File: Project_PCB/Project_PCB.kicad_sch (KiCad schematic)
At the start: 14 parts, among them J1 USB_C_Receptacle, J2 Conn_01x03_Socket, U1 ESP32-WROOM-32E

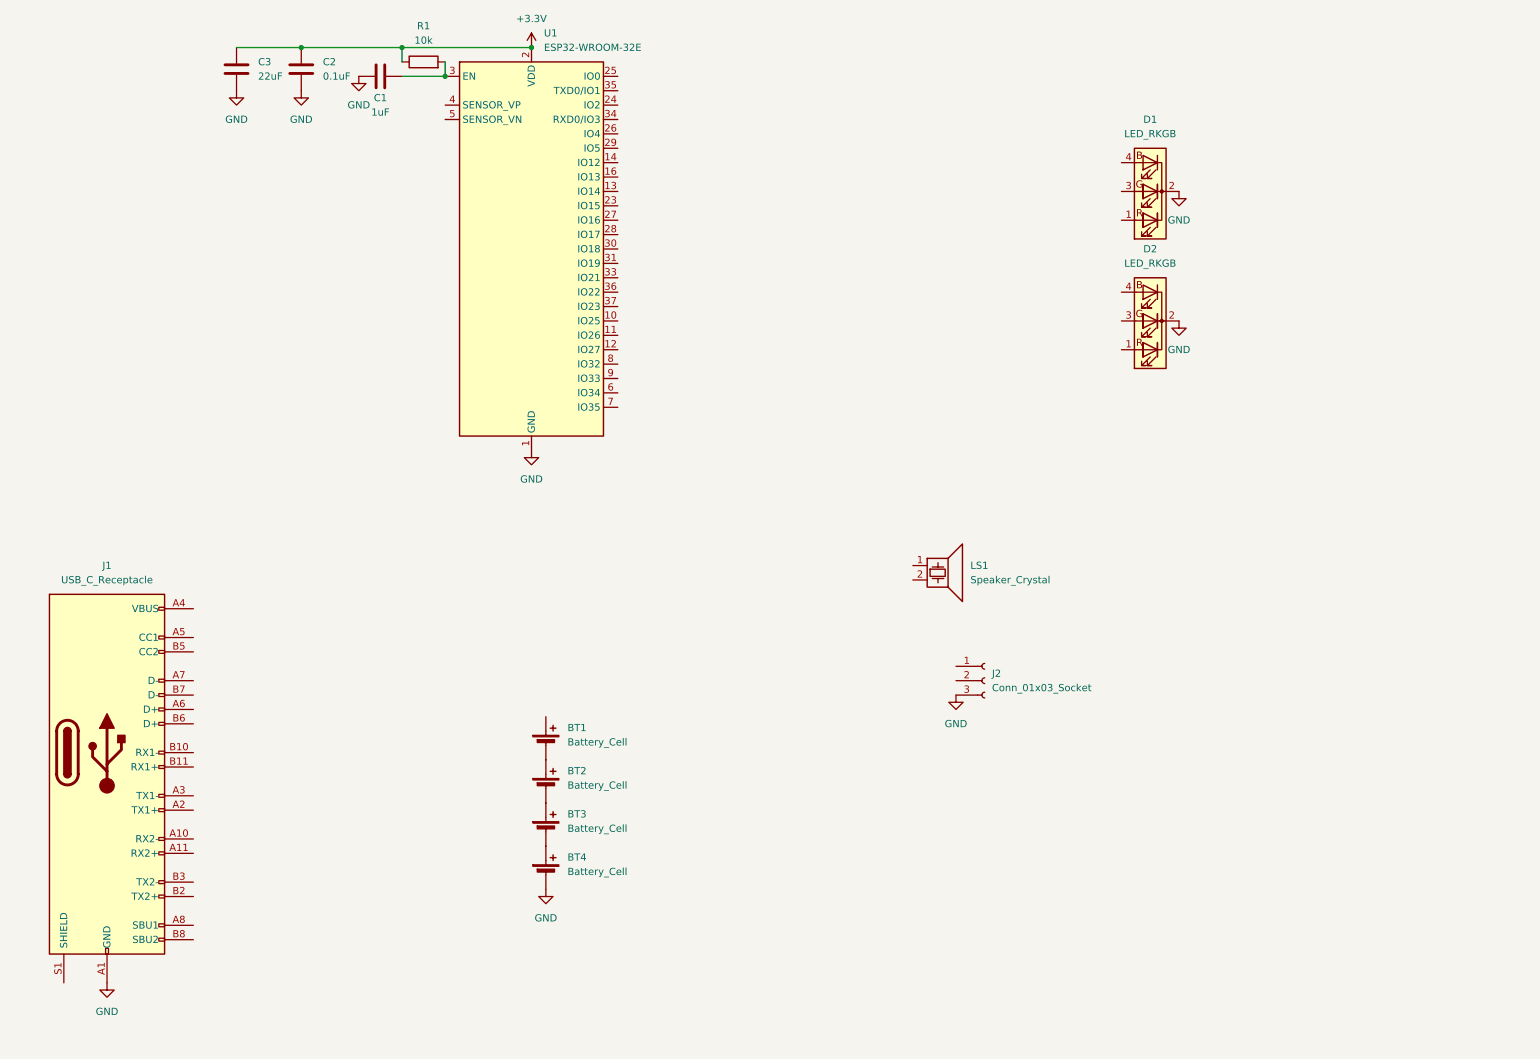
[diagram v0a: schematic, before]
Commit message: Changed mcu to ESP32-S3-WROOM-1 and updated some connections.
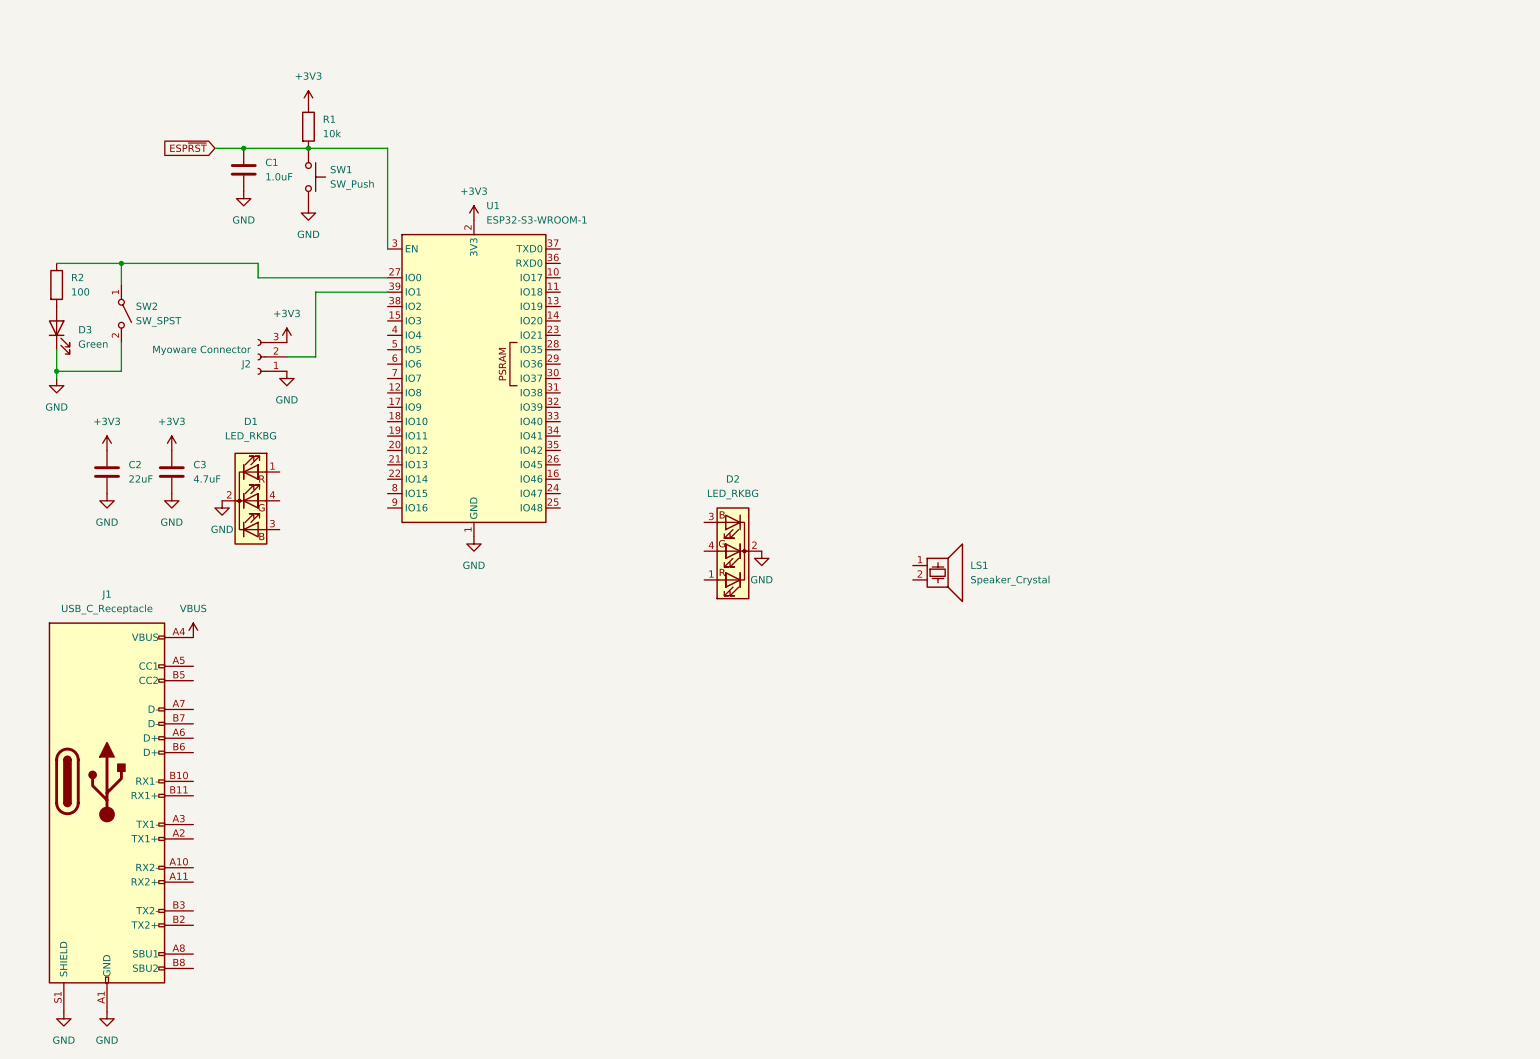
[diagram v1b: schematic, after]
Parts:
- removed BT1, BT2, BT3, BT4: Battery_Cell, symbol Device:Battery_Cell
- removed D1, D2: LED_RKGB, symbol Device:LED_RKGB
- removed U1: ESP32-WROOM-32E, RF_Module:ESP32-WROOM-32D, symbol RF_Module:ESP32-WROOM-32E
- added D1, D2: LED_RKBG, symbol Device:LED_RKBG
- added D3: Green, symbol Device:LED
- added R2: 100, symbol Device:R
- added SW1: SW_Push, symbol Switch:SW_Push
- added SW2: SW_SPST, symbol Switch:SW_SPST
- added U1: ESP32-S3-WROOM-1, RF_Module:ESP32-S3-WROOM-1, symbol RF_Module:ESP32-S3-WROOM-1
- C1: value 1uF -> 1.0uF
- C2: value 0.1uF -> 22uF
- C3: value 22uF -> 4.7uF
- J2: value Conn_01x03_Socket -> Myoware Connector
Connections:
- net GND: now also C1.2, J1.S1 (SHIELD), J2.1 (Pin_1), D1.2 (K), D2.2 (K), D3.1 (K), SW1.2, SW2.2 (B), U1.1 (GND), U1.40 (GND), U1.41 (GND); no longer C1.1, J2.3 (Pin_3)
- net ESP~{RST}: now reaches R1.2
- net ESP~{RST}: now also C1.1, SW1.1, U1.3 (EN); no longer C1.2
- net VBUS: now reaches J1.A4 (VBUS), J1.A9 (VBUS), J1.B4 (VBUS), J1.B9 (VBUS)
- net at J2.2 (Pin_2): now also U1.39 (IO1)
- net +3.3V renamed +3V3
- net +3V3: now also J2.3 (Pin_3), U1.2 (3V3)
- new net: D3.2 (A), R2.2
- new net: R2.1, SW2.1 (A), U1.27 (IO0)
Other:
- moved on the sheet: J1, J2

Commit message: minor updates to schematic
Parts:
- added R3, R4: 5k1, symbol Device:R
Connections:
- net GND: now also R3.2, R4.2
- net ESP19/D-: now reaches U1.13 (IO19)
- net ESP19/D-: now also J1.A7 (D-)
- net ESP20/D+: now reaches U1.14 (IO20)
- net ESP20/D+: now also J1.A6 (D+)
- net at J1.A5 (CC1): now also R3.1
- net at J1.B5 (CC2): now also R4.1

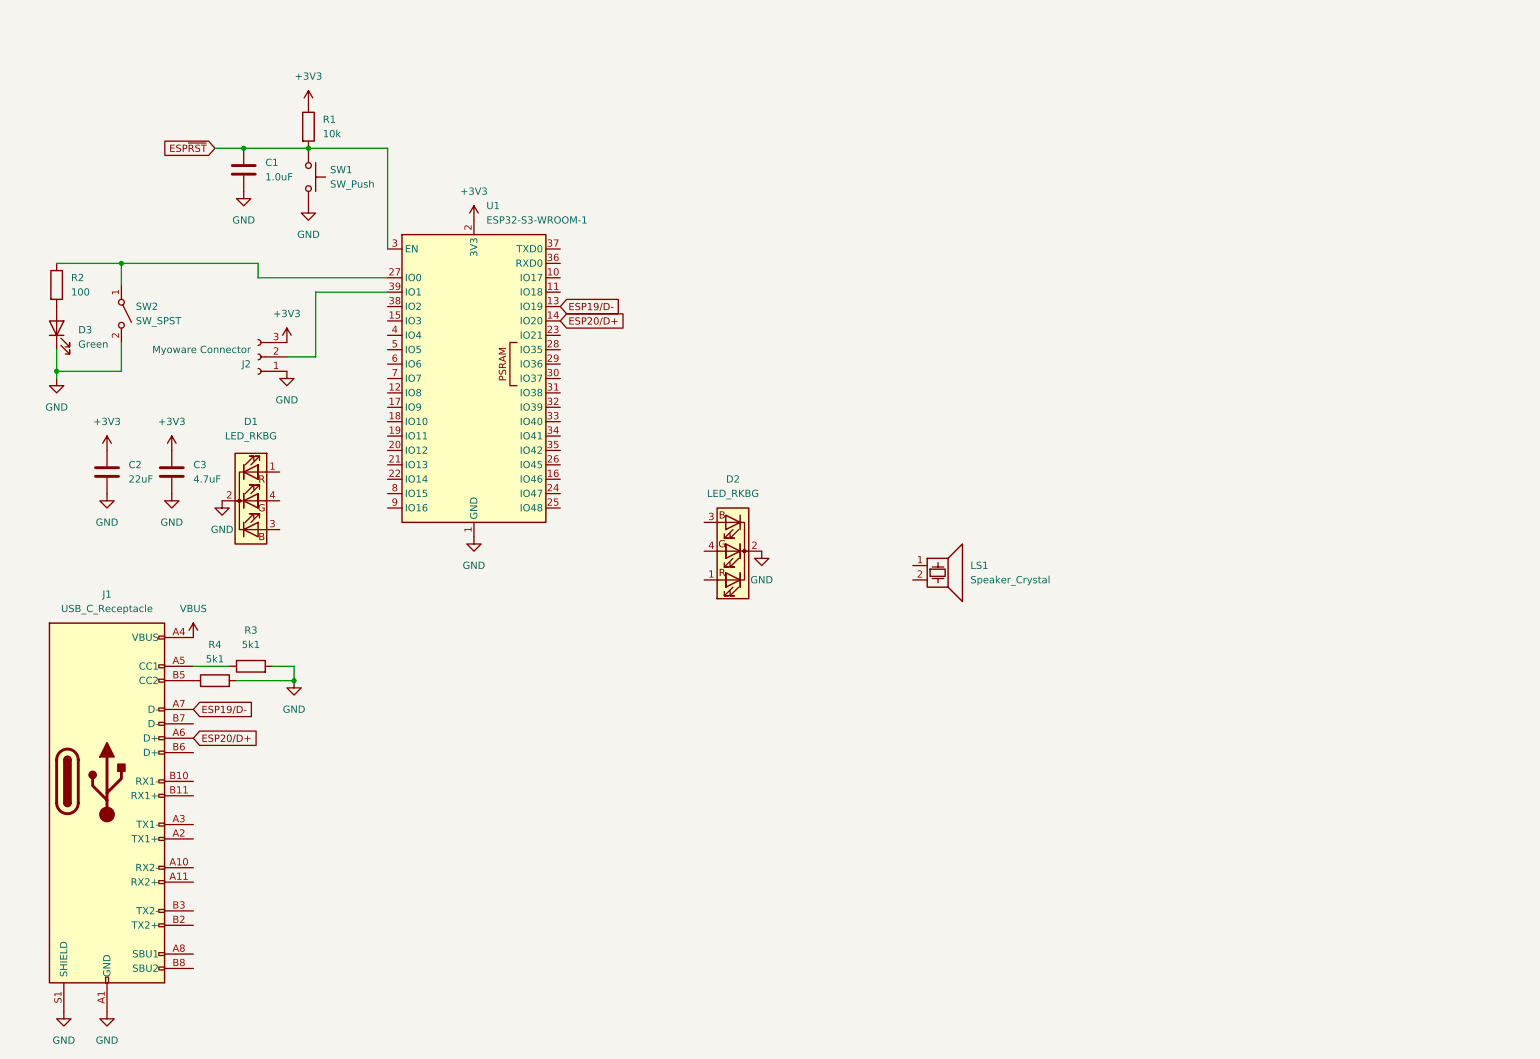
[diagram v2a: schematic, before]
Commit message: Most of ESP module finished
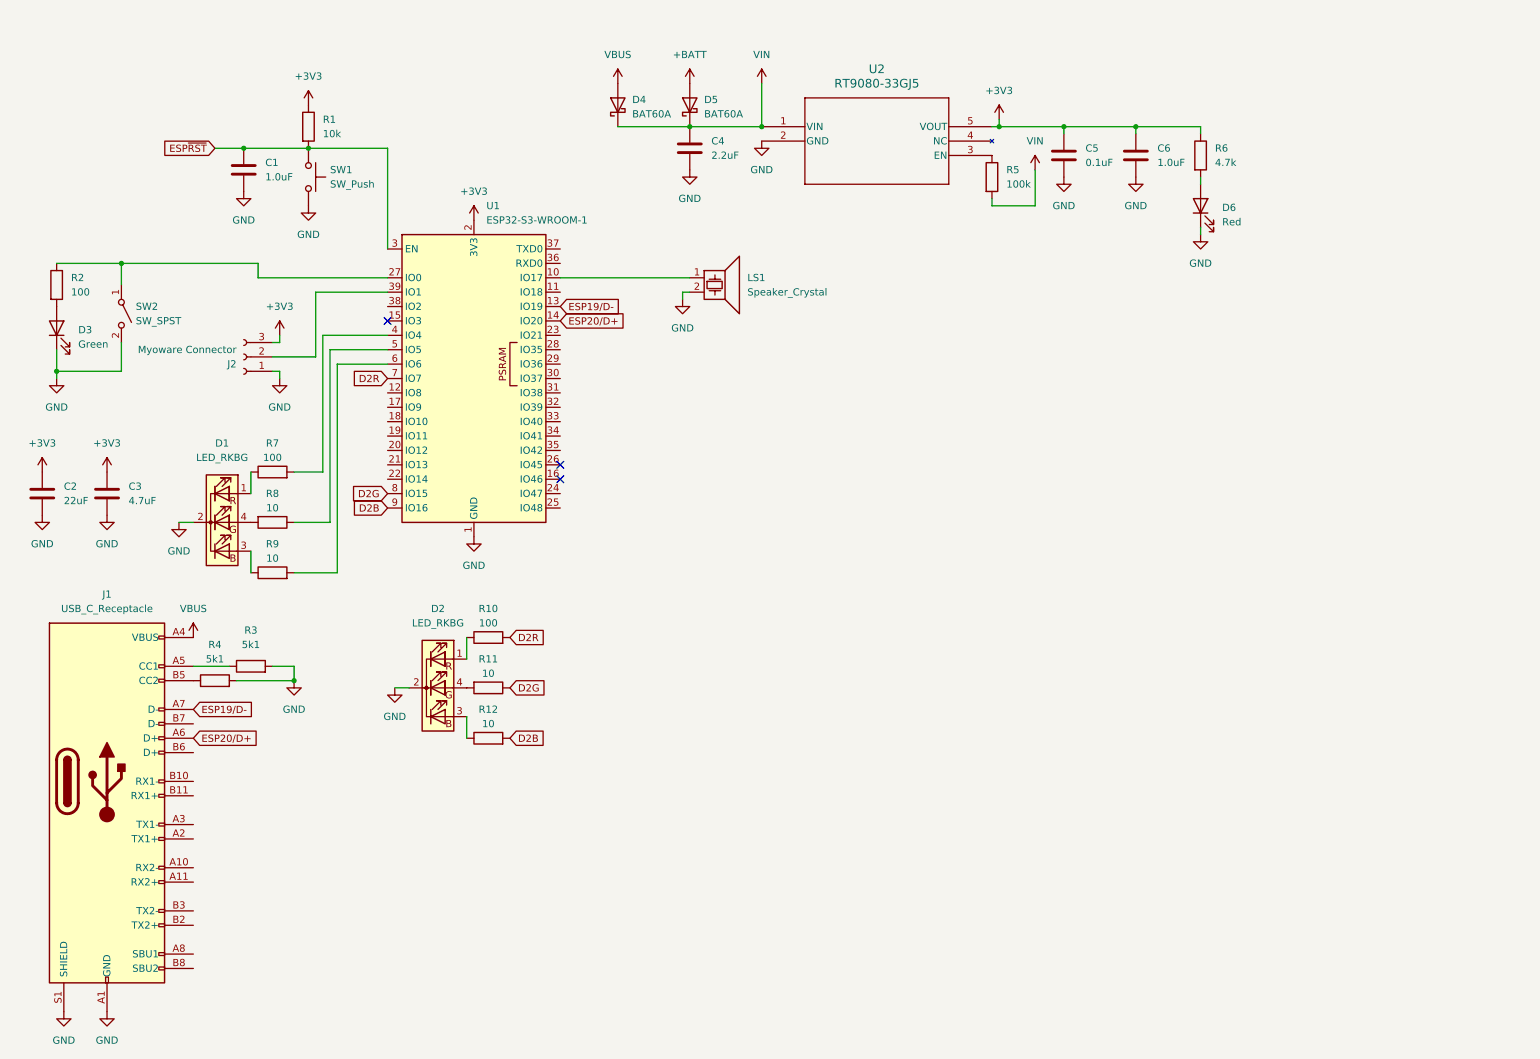
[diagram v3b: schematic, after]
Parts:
- added C4: 2.2uF, symbol Device:C
- added C5: 0.1uF, symbol Device:C
- added C6: 1.0uF, symbol Device:C
- added D4, D5: BAT60A, Diode_SMD:D_SOD-323, symbol Diode:BAT60A
- added D6: Red, symbol Device:LED
- added R10, R7: 100, symbol Device:R
- added R11, R12, R8, R9: 10, symbol Device:R
- added R5: 100k, symbol Device:R
- added R6: 4.7k, symbol Device:R
- added U2: RT9080-33GJ5, TSOT-23-5_RIT, symbol 2025-05-07_10-35-02:RT9080-33GJ5
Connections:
- net +3V3: now also C5.1, C6.1, R6.1, U2.5 (VOUT)
- net GND: now also LS1.2, C4.2, C5.2, C6.2, D6.1 (K), U2.2 (GND)
- net VBUS: now also D4.2 (A)
- net at LS1.1: now also U1.10 (IO17)
- net at U1.4 (IO4): now also R7.2
- net at U1.5 (IO5): now also R8.1
- net at U1.6 (IO6): now also R9.2
- net D2R: now reaches U1.7 (IO7)
- net D2R: now also R10.2
- net D2G: now reaches U1.8 (IO15)
- net D2G: now also R11.1
- net D2B: now reaches U1.9 (IO16)
- net D2B: now also R12.2
- net at D2.1 (RA): now also R10.1
- net at D2.3 (BA): now also R12.1
- net at D2.4 (GA): now also R11.2
- net at D1.1 (RA): now also R7.1
- net at D1.3 (BA): now also R9.1
- net at D1.4 (GA): now also R8.2
- new net: D6.2 (A), R6.2
- new net: R5.1, U2.3 (EN)
- new net +BATT: D5.2 (A)
- new net VIN: C4.1, D4.1 (K), D5.1 (K), R5.2, U2.1 (VIN)
- no-connect marks 0 -> 3
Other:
- moved on the sheet: C2, C3, D1, J2, LS1

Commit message: Finished initial version of schematic
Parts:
- added BT1: Battery_Cell, symbol Device:Battery_Cell
- added C7: 10uF, symbol Device:C
- added C8: 0.1uF, symbol Device:C
- added CR1: SMF05C.TCT, SC70-6L_SEM, symbol SMF05C:SMF05C.TCT
- added D7: Yellow, symbol Device:LED
- added J3: Conn_01x02, Connector_JST:JST_PH_S2B-PH-K_1x02_P2.00mm_Horizontal, symbol Connector_Generic:Conn_01x02
- added R13: 470, symbol Device:R
- added R14: 2.2k, symbol Device:R
- added U3: MCP73831T-2ACI/OT, SOT-23-5_MC_MCH, symbol MCP73831:MCP73831T-2ACI_OT
- added U4: MAX17048G+, 21-0168_T822+3_MXM, symbol MAX17048G:MAX17048G+
- R6: value 4.7k -> 1k
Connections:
- net +BATT: now also BT1.1 (+), C7.1, C8.1, J3.1 (Pin_1), U3.3 (VBAT), U4.2 (CELL), U4.3 (VDD)
- net ESP19/D-: now also J1.B7 (D-), CR1.6
- net ESP20/D+: now also J1.B6 (D+), CR1.5
- net GND: now also BT1.2 (-), C7.2, C8.2, CR1.2, J3.2 (Pin_2), R14.2, U3.2 (VSS), U4.1 (CTG), U4.4 (GND), U4.6 (QSTRT), U4.9 (EPAD)
- net VBUS: now also CR1.4, D7.2 (A), U3.4 (VDD)
- net ESP8/SDA: now reaches U1.12 (IO8)
- net ESP8/SDA: now also U4.8 (SDA)
- net ESP9/SCL: now reaches U1.17 (IO9)
- net ESP9/SCL: now also U4.7 (SCL)
- net ESP35/~{ALRT}: now reaches U1.28 (IO35)
- net ESP35/~{ALRT}: now also U4.5 (*ALRT)
- new net: R13.2, U3.1 (STAT)
- new net: R14.1, U3.5 (PROG)
- new net: D7.1 (K), R13.1
- no-connect marks 3 -> 13
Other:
- moved on the sheet: D2, LS1, R10, R11, R12, U1
